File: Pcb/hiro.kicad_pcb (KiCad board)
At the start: 2 copper layers, 92.9 x 60.4 mm, 11 parts, among them J1 Micro_SD_Card_Det_Hirose_DM3AT, J2 AudioJack3, J3 Conn_01x09, U1 XIAO-ESP32-S3-Plus-SMD, U2 PCM5102A

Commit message: THE OUTLINE WORKS YAYYY
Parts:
- C1, C2, C3, C4, C5, C6: footprint Capacitor_SMD:C_01005_0402Metric_Pad0.57x0.30mm_HandSolder -> Capacitor_SMD:C_0603_1608Metric_Pad1.08x0.95mm_HandSolder
- J3: value Conn_01x09 -> Conn_01x08; footprint Libs:Waveshare 2.4_ lcd -> Connector_PinHeader_2.54mm:PinHeader_1x08_P2.54mm_Vertical
- moved J3 163.2 mm to (58.7, 50.0)
- moved C3 148.8 mm to (58.0, 114.2), turned to -90 degrees
- moved C5 148.7 mm to (59.4, 111.8)
- moved C1 148.4 mm to (59.2, 121.0)
- moved C6 147.0 mm to (62.5, 121.0)
- moved U2 146.9 mm to (62.2, 116.4)
- moved C2 145.3 mm to (65.9, 121.0)
- moved C4 145.1 mm to (64.6, 111.6), turned to 0 degrees
- moved J2 132.4 mm to (61.9, 133.3), turned to 180 degrees
- moved U1 101.8 mm to (85.7, 129.8), turned to -90 degrees
- moved J1 67.7 mm to (118.8, 42.6), turned to 180 degrees
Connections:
- J3 pad 1: unconnected-(J3-Pin_1-Pad1) -> +3.3V
- J3 pad 2: unconnected-(J3-Pin_2-Pad2) -> GND
- J3 pad 3: unconnected-(J3-Pin_3-Pad3) -> /DIN
- J3 pad 4: unconnected-(J3-Pin_4-Pad4) -> /CLK
- J3 pad 5: unconnected-(J3-Pin_6-Pad6) -> /CS
- J3 pad 6: unconnected-(J3-Pin_7-Pad7) -> /DC
- J3 pad 7: unconnected-(J3-Pin_8-Pad8) -> /RST
- J3 pad 8: Net-(J3-Pin_9) -> /BL
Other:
- board size 92.9 x 60.4 mm -> 80.1 x 107.1 mm

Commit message: New wiring cause botato is awesome
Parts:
- added S1: B3U-3100P-B, Button_Switch_SMD:SW_SPST_B3U-3100P, F.Cu at (129.7, 63.9)
- added S2: B3U-3100P-B, Button_Switch_SMD:SW_SPST_B3U-3100P, F.Cu at (129.6, 101.0)
- added S3: B3U-3100P-B, Button_Switch_SMD:SW_SPST_B3U-3100P, F.Cu at (102.0, 81.6)
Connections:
- net /DIN renamed /DIN1
- J1 pad 2: unconnected-(J1-DAT3/CD-Pad2) -> /SD_CS
- J1 pad 3: unconnected-(J1-CMD-Pad3) -> /CMD
- J1 pad 4: unconnected-(J1-VDD-Pad4) -> +3.3V
- J1 pad 6: unconnected-(J1-VSS-Pad6) -> GND
- J1 pad 7: unconnected-(J1-DAT0-Pad7) -> /DAT0
- J1 pad SH: unconnected-(J1-SHIELD-PadSH) -> GND
- U1 pad 1: unconnected-(U1-GPIO1_A0_D0-Pad1) -> /SD_CS
- U1 pad 15: unconnected-(U1-GPIO38_DVP_VSYNC_I2S_SD-Pad15) -> /DIN2
- U1 pad 16: unconnected-(U1-GPIO39_CAM_SCL_I2S_SCK-Pad16) -> /BCK
- U1 pad 17: unconnected-(U1-GPIO40_CAM_SDA_I2S_WS-Pad17) -> /LCK
- U1 pad 2: unconnected-(U1-GPIO2_A1_D1-Pad2) -> /CMD
- U1 pad 25: unconnected-(U1-GPIO40_MTDO_CAM_SDA_I2S_WS-Pad25) -> /SW3
- U1 pad 27: unconnected-(U1-GND1-Pad27) -> GND
- U1 pad 28: unconnected-(U1-GPIO42_MTMS_PDM_CLK_TX1-Pad28) -> /SW2
- U1 pad 29: unconnected-(U1-GPIO39_MTCK_CAM_SCL_I2S_SCK-Pad29) -> /SW1
- U1 pad 3: unconnected-(U1-GPIO3_A2_D2-Pad3) -> /CLK

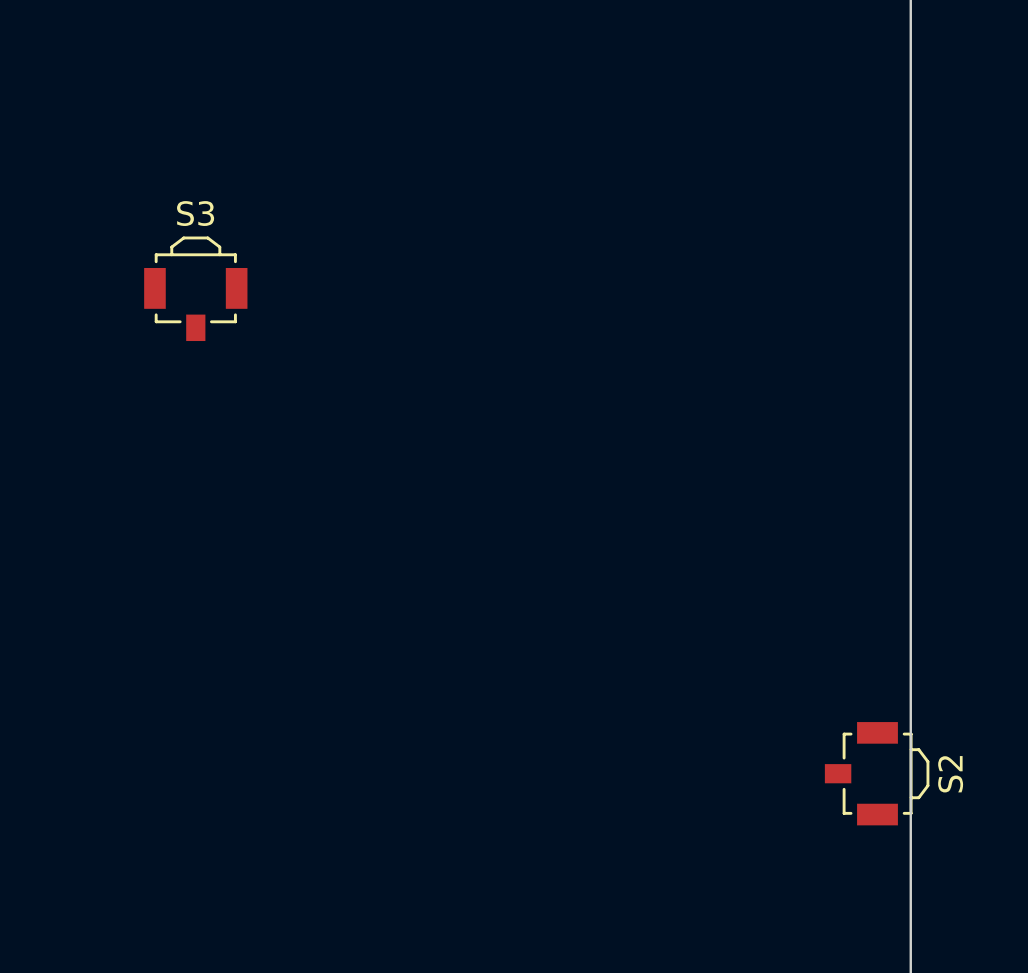
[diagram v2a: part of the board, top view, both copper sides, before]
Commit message: got a sideway switch working correctly.
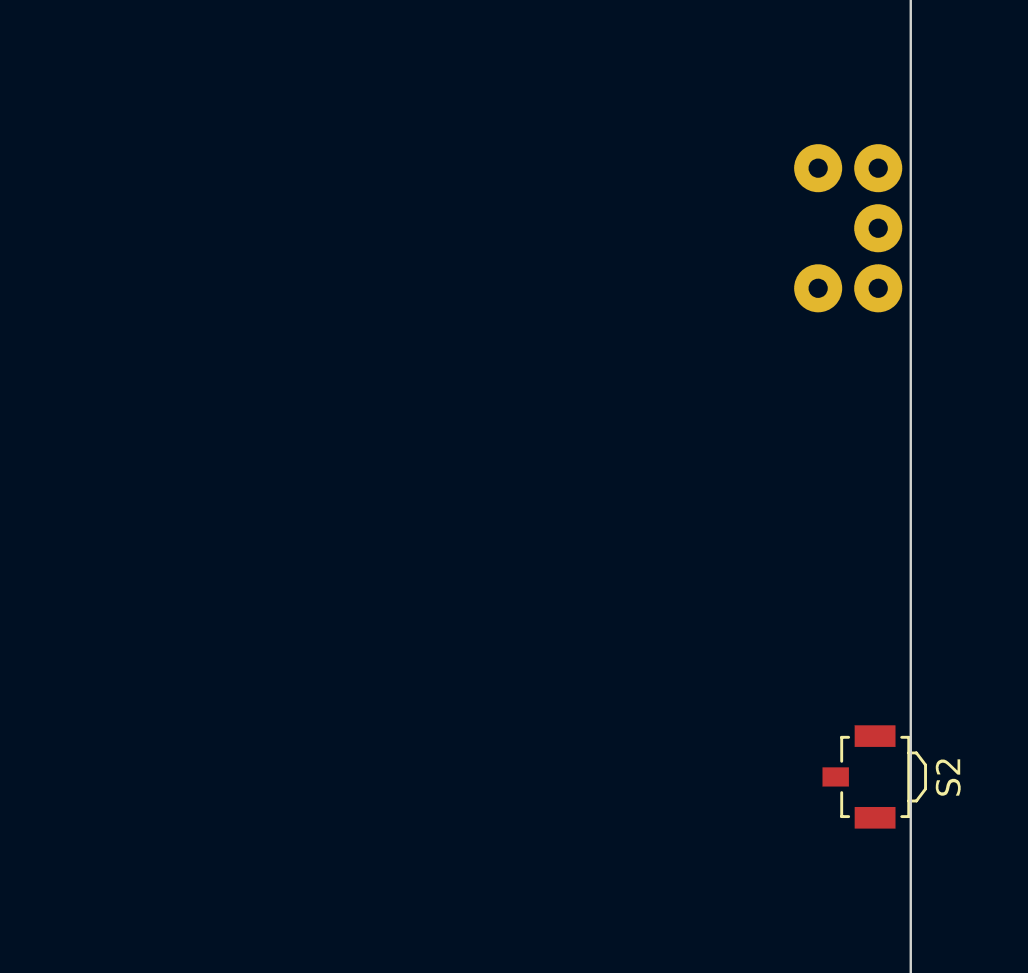
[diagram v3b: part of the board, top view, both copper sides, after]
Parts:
- removed S3: B3U-3100P-B, Button_Switch_SMD:SW_SPST_B3U-3100P
- added SW1: RotaryEncoder_Switch, Libs:Right angle EC11 Rotary Encoder, F.Cu at (130.4, 80.8)
- moved S2 0.17 mm to (129.5, 101.2)
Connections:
- net /BL renamed /MISO
- net /RST renamed /MOSI
- J1 pad 2: /SD_CS -> unconnected-(J1-DAT3/CD-Pad2)
- J1 pad 3: /CMD -> unconnected-(J1-CMD-Pad3)
- J1 pad 5: unconnected-(J1-CLK-Pad5) -> /CLK
- J1 pad 7: /DAT0 -> unconnected-(J1-DAT0-Pad7)
- U1 pad 1: /SD_CS -> /ENCA
- U1 pad 2: /CMD -> /ENCB
- U1 pad 3: /CLK -> unconnected-(U1-GPIO3_A2_D2-Pad3)

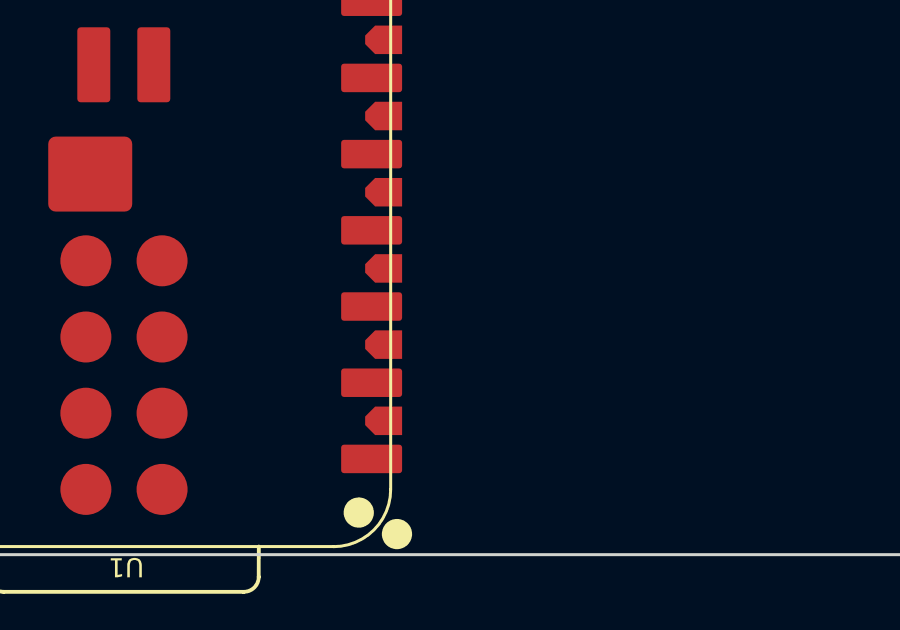
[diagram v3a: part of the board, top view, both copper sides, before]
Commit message: Speaker + Speaker amp and 3d model
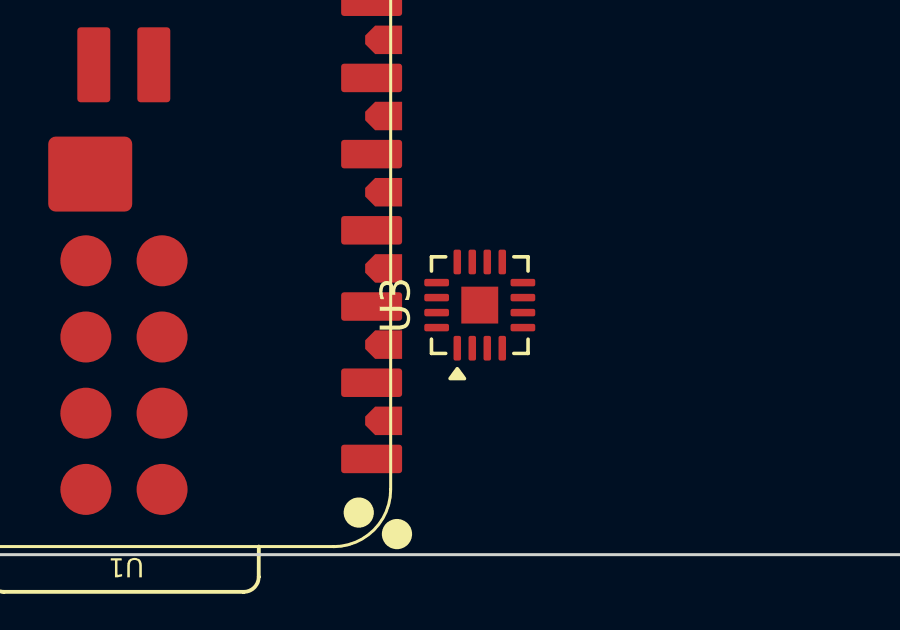
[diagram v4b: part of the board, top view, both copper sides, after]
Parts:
- added U3: MAX98357A, Package_DFN_QFN:TQFN-16-1EP_3x3mm_P0.5mm_EP1.23x1.23mm, F.Cu at (97.6, 132.3)
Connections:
- net /CLK renamed /SCK
- J1 pad 2: unconnected-(J1-DAT3/CD-Pad2) -> /CS
- J1 pad 3: unconnected-(J1-CMD-Pad3) -> /MOSI
- J1 pad 7: unconnected-(J1-DAT0-Pad7) -> /MISO
- U1 pad 32: unconnected-(U1-VBAT-Pad32) -> Net-(BT1-+)
- U1 pad 33: unconnected-(U1-GND2-Pad33) -> Net-(BT1--)

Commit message: Some stuffs
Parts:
- added LS2: CVS-3108, Spkr:CUI_CVS-3108, F.Cu at (91.8, 100.2)
- moved J1 8.81 mm to (110.0, 42.4)
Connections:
- J1 pad 2: /CS -> /CS1
- U1 pad 23: unconnected-(U1-GPIO13_DVP_PCLK_SPI_SCK1-Pad23) -> /CS1
- U3 pad 17: unconnected-(U3-PAD-Pad17) -> GND
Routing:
- net /SCK: track 0.00 -> 80.3 mm, vias 0 -> 1
- net /DC: track 0.00 -> 67.3 mm, vias 0 -> 1
- net /MOSI: track 0.00 -> 66.0 mm, vias 0 -> 1
- net GND: track 0.00 -> 57.3 mm, vias 0 -> 3
- net /BCK: track 0.00 -> 46.6 mm, vias 0 -> 2
- net Net-(U3-OUTP): track 0.00 -> 37.1 mm, vias 0 -> 1
- net Net-(U3-OUTN): track 0.00 -> 31.8 mm
- net +3.3V: track 0.00 -> 29.8 mm
- net /DIN1: track 0.00 -> 26.3 mm
- net Net-(U2-OUTR): track 0.00 -> 17.8 mm
- net Net-(U2-OUTL): track 0.00 -> 14.7 mm
- net Net-(U2-CAPP): track 0.00 -> 2.81 mm
- net Net-(U2-CAPM): track 0.00 -> 2.38 mm
- net Net-(U2-AVDD): track 0.00 -> 2.26 mm
- net /LCK: track 0.00 -> 2.17 mm
- added copper zone on B.Cu, net GND
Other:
- outline, holes or cut-outs redrawn

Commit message: New Speaker, some new cad, other stuff, renders, etc
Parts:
- removed LS2: CVS-3108, Spkr:CUI_CVS-3108
- added J4: Conn_01x02, Connector_JST:JST_PH_S2B-PH-K_1x02_P2.00mm_Horizontal, F.Cu at (59.2, 96.2)
- added LS1: CVS-1708, Spkr:SPKR_CVS-1708, F.Cu at (77.5, 47.5)
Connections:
- J1 pad 2: /CS1 -> Net-(J1-DAT3/CD)
- J1 pad 3: /MOSI -> Net-(J1-CMD)
- J1 pad 4: +3.3V -> Net-(J1-VDD)
- J1 pad 5: /SCK -> Net-(J1-CLK)
- J1 pad 7: /MISO -> Net-(J1-DAT0)
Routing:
- net Net-(U3-OUTN): track 31.8 -> 93.1 mm, vias 0 -> 1
- net Net-(U3-OUTP): track 37.1 -> 94.2 mm, vias 1 -> 2
- net Net-(J4-Pin_2): track 0.00 -> 41.9 mm, vias 0 -> 1
- net /DIN2: track 0.00 -> 41.0 mm, vias 0 -> 2
- net Net-(J4-Pin_1): track 0.00 -> 40.8 mm, vias 0 -> 1
- net /LCK: track 2.17 -> 42.3 mm, vias 0 -> 2
- net GND: track 57.3 -> 86.9 mm, vias 3 -> 4
- net +3.3V: track 29.8 -> 33.5 mm
- net Net-(U2-DVDD): track 0.00 -> 2.07 mm
- net Net-(U2-VNEG): track 0.00 -> 1.90 mm
- net Net-(U2-LDOO): track 0.00 -> 1.90 mm

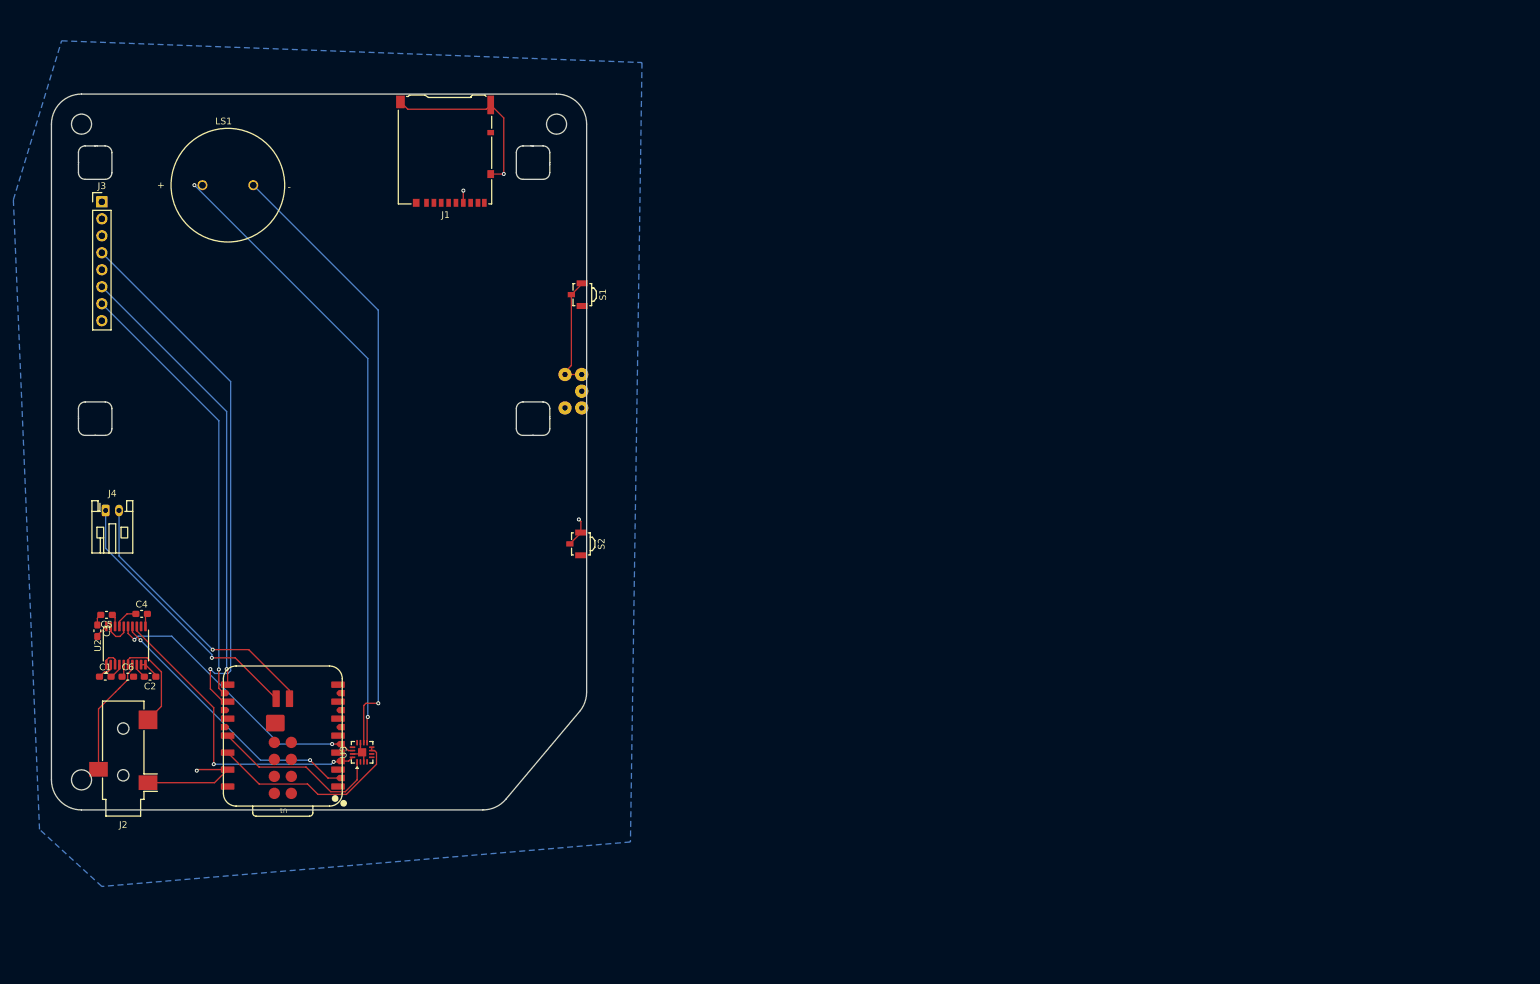
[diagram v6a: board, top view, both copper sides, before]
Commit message: Placed The screen connector in (almost) the right spot
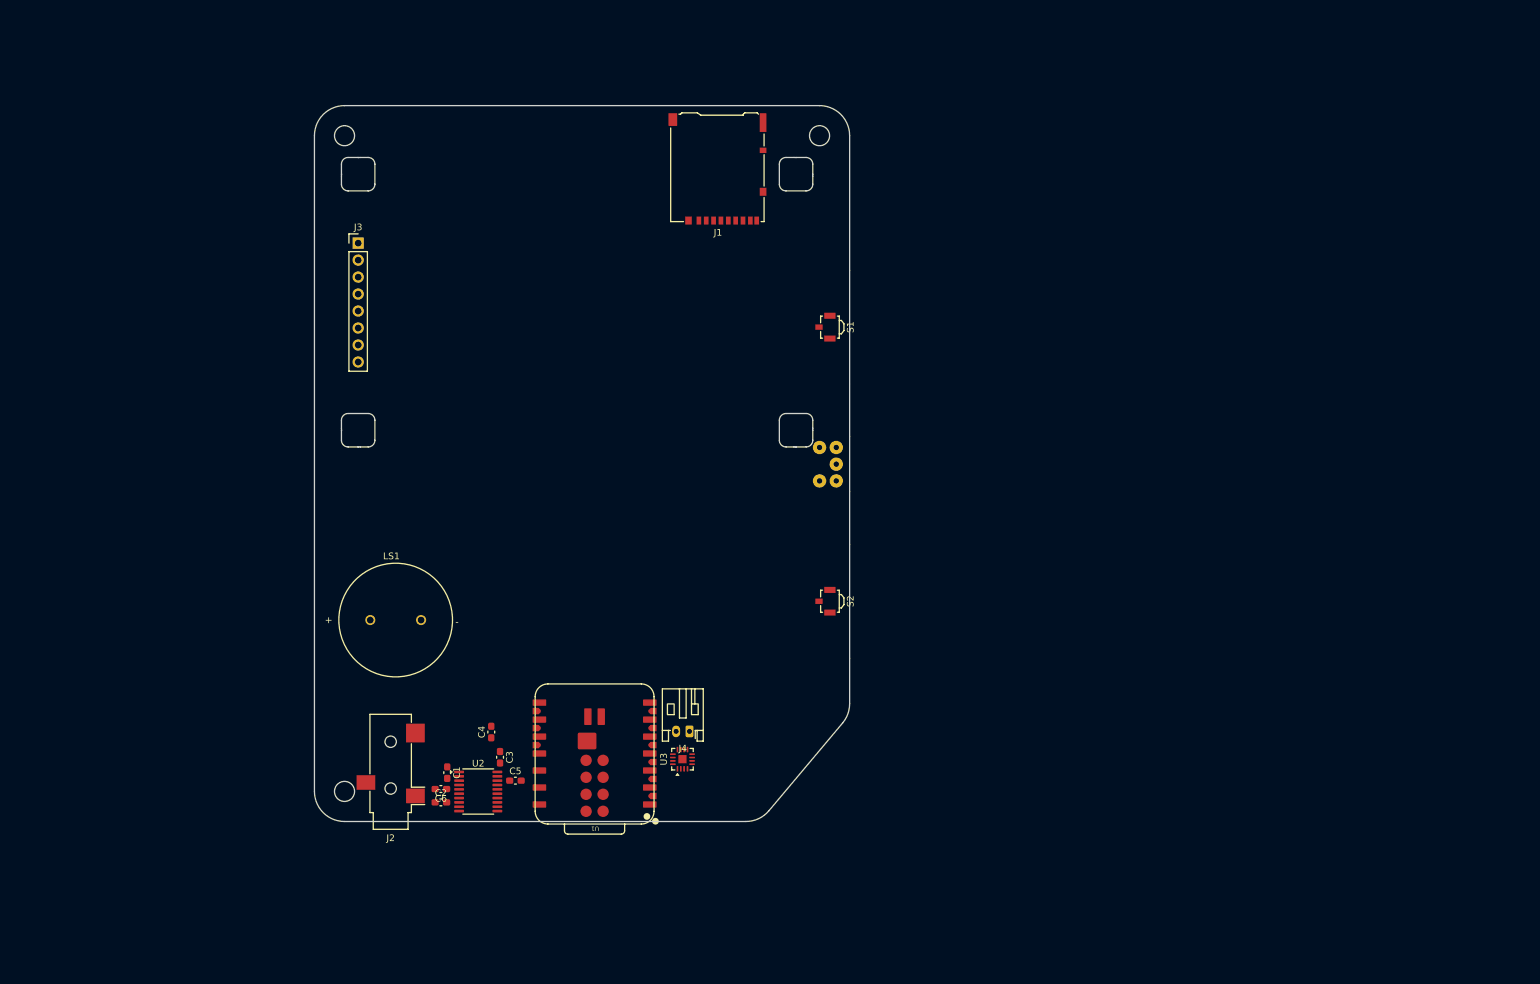
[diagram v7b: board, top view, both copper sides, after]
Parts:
- moved J4 93.4 mm to (146.6, 129.2), turned to 180 degrees
- moved LS1 69.7 mm to (102.6, 112.5)
- moved C5 66.0 mm to (120.5, 136.6), turned to 0 degrees
- moved C3 63.1 mm to (118.2, 133.1)
- moved U2 57.0 mm to (115.0, 138.2), turned to 0 degrees
- moved C4 55.2 mm to (116.9, 129.3), turned to 90 degrees
- moved C1 53.1 mm to (110.3, 135.4), turned to -90 degrees
- moved C6 49.8 mm to (109.4, 137.8), turned to 180 degrees
- moved U3 47.9 mm to (145.5, 133.4)
- moved C2 47.4 mm to (109.4, 139.8), turned to 0 degrees
- moved U1 46.7 mm to (132.4, 132.5)
- moved J1 40.8 mm to (150.7, 45.1)
- moved J2 40.0 mm to (101.8, 135.2)
- moved SW1 39.6 mm to (168.5, 91.7)
- moved J3 38.8 mm to (97.0, 56.2)
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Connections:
- J1 pad 2: Net-(J1-DAT3/CD) -> /CS1
- J1 pad 3: Net-(J1-CMD) -> /MOSI
- J1 pad 4: Net-(J1-VDD) -> +3.3V
- J1 pad 5: Net-(J1-CLK) -> /SCK
- J1 pad 7: Net-(J1-DAT0) -> /MISO
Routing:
- net Net-(U3-OUTP): track 94.2 -> 0.00 mm, vias 2 -> 0
- net Net-(U3-OUTN): track 93.1 -> 0.00 mm, vias 1 -> 0
- net GND: track 86.9 -> 0.00 mm, vias 4 -> 0
- net /SCK: track 80.3 -> 0.00 mm, vias 1 -> 0
- net /DC: track 67.3 -> 0.00 mm, vias 1 -> 0
- net /MOSI: track 66.0 -> 0.00 mm, vias 1 -> 0
- net /BCK: track 46.6 -> 0.00 mm, vias 2 -> 0
- net /LCK: track 42.3 -> 0.00 mm, vias 2 -> 0
- net Net-(J4-Pin_2): track 41.9 -> 0.00 mm, vias 1 -> 0
- net /DIN2: track 41.0 -> 0.00 mm, vias 2 -> 0
- net Net-(J4-Pin_1): track 40.8 -> 0.00 mm, vias 1 -> 0
- net +3.3V: track 33.5 -> 0.00 mm
- net /DIN1: track 26.3 -> 0.00 mm
- net Net-(U2-OUTR): track 17.8 -> 0.00 mm
- net Net-(U2-OUTL): track 14.7 -> 0.00 mm
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- removed copper zone on B.Cu, net GND
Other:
- outline, holes or cut-outs redrawn

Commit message: Lots of wiring
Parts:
- moved C4 6.94 mm to (122.0, 134.0)
- moved J2 1.26 mm to (102.0, 134.0)
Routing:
- net GND: track 0.00 -> 168.4 mm, vias 0 -> 10
- net /MOSI: track 0.00 -> 136.4 mm, vias 0 -> 2
- net /MISO: track 0.00 -> 129.2 mm, vias 0 -> 2
- net /SCK: track 0.00 -> 128.8 mm, vias 0 -> 2
- net /DIN1: track 0.00 -> 107.5 mm, vias 0 -> 3
- net +3.3V: track 0.00 -> 101.1 mm, vias 0 -> 2
- net /CS1: track 0.00 -> 98.2 mm
- net /CS: track 0.00 -> 77.4 mm, vias 0 -> 1
- net /DC: track 0.00 -> 76.7 mm, vias 0 -> 1
- net /SW3: track 0.00 -> 73.8 mm
- net /ENCA: track 0.00 -> 66.0 mm, vias 0 -> 2
- net /ENCB: track 0.00 -> 62.8 mm, vias 0 -> 2
- net Net-(U3-OUTP): track 0.00 -> 55.6 mm, vias 0 -> 1
- net /SW2: track 0.00 -> 50.3 mm
- net Net-(U3-OUTN): track 0.00 -> 48.8 mm, vias 0 -> 1
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- added copper zone on F.Cu, net +3.3V
- added copper zone on B.Cu, net GND
